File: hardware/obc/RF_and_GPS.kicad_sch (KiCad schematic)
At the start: 15 parts, among them J602 SMA RA Connector, J603 SMA RA Connector, J604 SMA RA Connector, U102 BMI088, U601 RFM98PW, U602 S1216V8, U603 GP2S1+

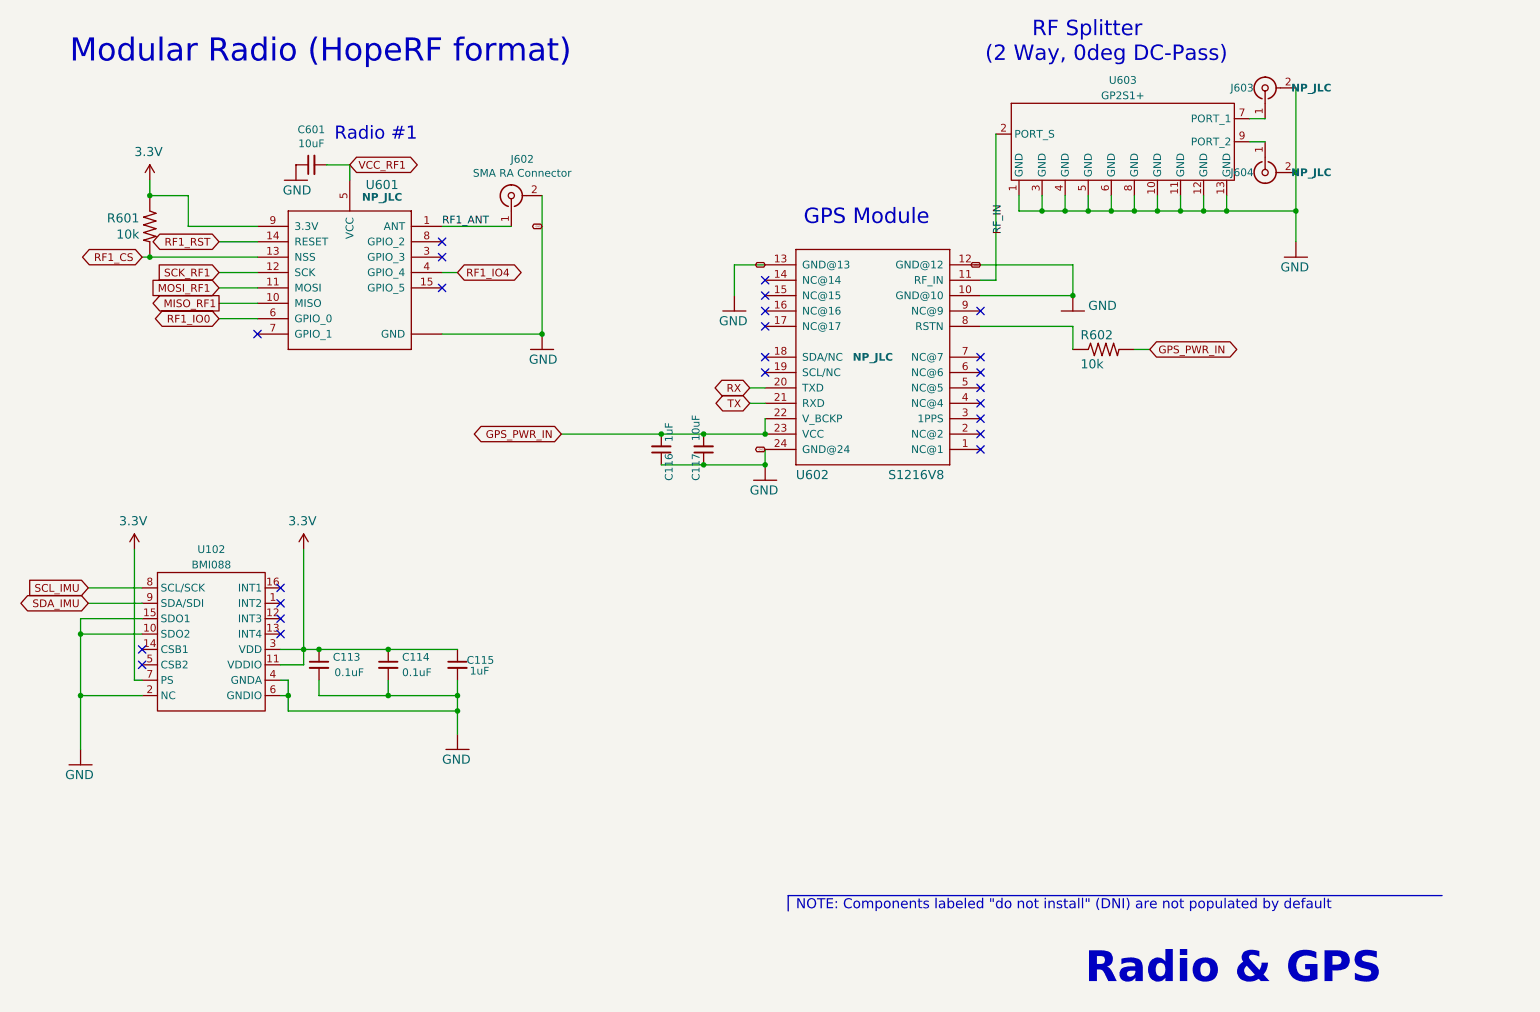
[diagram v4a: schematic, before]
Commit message: obc: refactors and renumbers
- renumber pages for more logical review order
- renumber reference designators to get smaller numbers
- small changes to layout from early design review
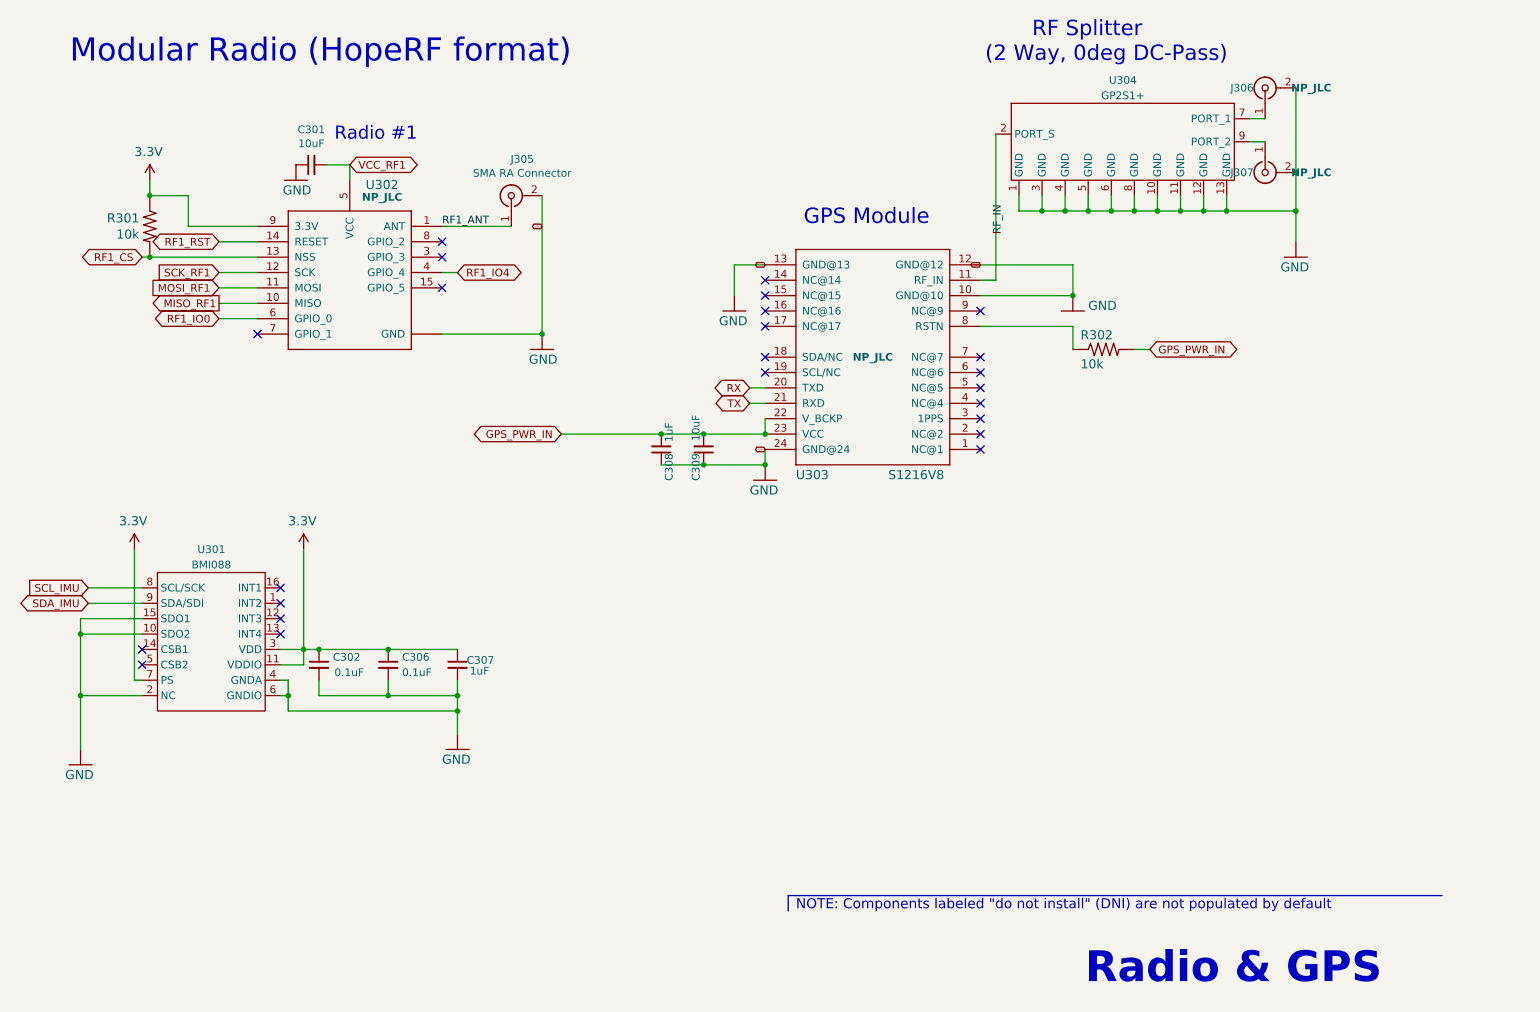
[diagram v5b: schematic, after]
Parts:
- renumbered C601 to C301, C113 to C302, C114 to C306, C115 to C307, C116 to C308, C117 to C309, J602 to J305, J603 to J306, J604 to J307, R601 to R301, R602 to R302, U102 to U301, U601 to U302, U602 to U303, U603 to U304
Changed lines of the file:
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@@
 		(on_board yes)
 		(dnp no)
-		(property "Reference" "R602"
+		(property "Reference" "R302"
 			(at 207.01 77.2414 0)
 			(effects
@@
 			(project "mainboard"
 				(path "/e3ac22ea-6806-4807-a025-571315789c25/00000000-0000-0000-0000-00005cec6281"
-					(reference "R602")
+					(reference "R302")
 					(unit 1)
 				)
@@
 		(on_board yes)
 		(dnp no)
-		(property "Reference" "#GND0607"
+		(property "Reference" "#GND0309"
 			(at 242.57 63.5 0)
 			(effects
@@
 			(project "mainboard"
 				(path "/e3ac22ea-6806-4807-a025-571315789c25/00000000-0000-0000-0000-00005cec6281"
-					(reference "#GND0607")
+					(reference "#GND0309")
 					(unit 1)
 				)
@@
 		(on_board yes)
 		(dnp no)
-		(property "Reference" "J603"
+		(property "Reference" "J306"
 			(at 233.68 35.56 90)
 			(effects
@@
 			(project "mainboard"
 				(path "/e3ac22ea-6806-4807-a025-571315789c25/00000000-0000-0000-0000-00005cec6281"
-					(reference "J603")
+					(reference "J306")
 					(unit 1)
 				)
@@
 		(on_board yes)
 		(dnp no)
-		(property "Reference" "J604"
+		(property "Reference" "J307"
 			(at 233.68 49.53 90)
 			(effects
@@
 			(project "mainboard"
 				(path "/e3ac22ea-6806-4807-a025-571315789c25/00000000-0000-0000-0000-00005cec6281"
-					(reference "J604")
+					(reference "J307")
 					(unit 1)
 				)
@@
 		(on_board yes)
 		(dnp no)
-		(property "Reference" "J602"
+		(property "Reference" "J305"
 			(at 114.8334 47.3202 90)
 			(effects
@@
 			(project "mainboard"
 				(path "/e3ac22ea-6806-4807-a025-571315789c25/00000000-0000-0000-0000-00005cec6281"
-					(reference "J602")
+					(reference "J305")
 					(unit 1)
 				)
@@
 		(on_board yes)
 		(dnp no)
-		(property "Reference" "U601"
+		(property "Reference" "U302"
 			(at 91.694 51.562 0)
 			(effects
@@
 			(project "mainboard"
 				(path "/e3ac22ea-6806-4807-a025-571315789c25/00000000-0000-0000-0000-00005cec6281"
-					(reference "U601")
+					(reference "U302")
 					(unit 1)
 				)
@@
 		(on_board yes)
 		(dnp no)
-		(property "Reference" "#GND0603"
+		(property "Reference" "#GND0305"
 			(at 118.11 78.74 0)
 			(effects
@@
 			(project "mainboard"
 				(path "/e3ac22ea-6806-4807-a025-571315789c25/00000000-0000-0000-0000-00005cec6281"
-					(reference "#GND0603")
+					(reference "#GND0305")
 					(unit 1)
 				)
@@
 		(on_board yes)
 		(dnp no)
-		(property "Reference" "R601"
+		(property "Reference" "R301"
 			(at 51.6128 57.0738 90)
 			(effects
@@
 			(project "mainboard"
 				(path "/e3ac22ea-6806-4807-a025-571315789c25/00000000-0000-0000-0000-00005cec6281"
-					(reference "R601")
+					(reference "R301")
 					(unit 1)
 				)
@@
 		(on_board yes)
 		(dnp no)
-		(property "Reference" "#SUPPLY0601"
+		(property "Reference" "#SUPPLY0302"
 			(at 53.34 50.8 0)
 			(effects
@@
 			(project "mainboard"
 				(path "/e3ac22ea-6806-4807-a025-571315789c25/00000000-0000-0000-0000-00005cec6281"
-					(reference "#SUPPLY0601")
+					(reference "#SUPPLY0302")
 					(unit 1)
 				)
@@
 		(on_board yes)
 		(dnp no)
-		(property "Reference" "C601"
+		(property "Reference" "C301"
 			(at 80.01 42.4434 90)
 			(effects
@@
 			(project "mainboard"
 				(path "/e3ac22ea-6806-4807-a025-571315789c25/00000000-0000-0000-0000-00005cec6281"
-					(reference "C601")
+					(reference "C301")
 					(unit 1)
 				)
@@
 		(on_board yes)
 		(dnp no)
-		(property "Reference" "#GND0601"
+		(property "Reference" "#GND0302"
 			(at 77.47 50.8 0)
 			(effects
@@
 			(project "mainboard"
 				(path "/e3ac22ea-6806-4807-a025-571315789c25/00000000-0000-0000-0000-00005cec6281"
-					(reference "#GND0601")
+					(reference "#GND0302")
 					(unit 1)
 				)
@@
 		(on_board yes)
 		(dnp no)
-		(property "Reference" "#GND0604"
+		(property "Reference" "#GND0306"
 			(at 149.86 72.39 0)
 			(effects
@@
 			(project "mainboard"
 				(path "/e3ac22ea-6806-4807-a025-571315789c25/00000000-0000-0000-0000-00005cec6281"
-					(reference "#GND0604")
+					(reference "#GND0306")
 					(unit 1)
 				)
@@
 		(on_board yes)
 		(dnp no)
-		(property "Reference" "#GND0605"
+		(property "Reference" "#GND0307"
 			(at 154.94 100.33 0)
 			(effects
@@
 			(project "mainboard"
 				(path "/e3ac22ea-6806-4807-a025-571315789c25/00000000-0000-0000-0000-00005cec6281"
-					(reference "#GND0605")
+					(reference "#GND0307")
 					(unit 1)
 				)
@@
 		(on_board yes)
 		(dnp no)
-		(property "Reference" "#GND0606"
+		(property "Reference" "#GND0308"
 			(at 205.74 72.39 0)
 			(effects
@@
 			(project "mainboard"
 				(path "/e3ac22ea-6806-4807-a025-571315789c25/00000000-0000-0000-0000-00005cec6281"
-					(reference "#GND0606")
+					(reference "#GND0308")
 					(unit 1)
 				)
@@
 		(on_board yes)
 		(dnp no)
-		(property "Reference" "U602"
+		(property "Reference" "U303"
 			(at 160.02 100.33 0)
 			(effects
@@
 			(project "mainboard"
 				(path "/e3ac22ea-6806-4807-a025-571315789c25/00000000-0000-0000-0000-00005cec6281"
-					(reference "U602")
+					(reference "U303")
 					(unit 1)
 				)
@@
 		(on_board yes)
 		(dnp no)
-		(property "Reference" "C114"
+		(property "Reference" "C306"
 			(at 94.996 129.54 0)
 			(effects
@@
 			(project "mainboard"
 				(path "/e3ac22ea-6806-4807-a025-571315789c25/00000000-0000-0000-0000-00005cec6281"
-					(reference "C114")
+					(reference "C306")
 					(unit 1)
 				)
@@
 		(on_board yes)
 		(dnp no)
-		(property "Reference" "U102"
+		(property "Reference" "U301"
 			(at 63.5 111.76 0)
 			(effects
@@
 			(project "mainboard"
 				(path "/e3ac22ea-6806-4807-a025-571315789c25/00000000-0000-0000-0000-00005cec6281"
-					(reference "U102")
+					(reference "U301")
 					(unit 1)
 				)
@@
 		(dnp no)
 		(fields_autoplaced yes)
-		(property "Reference" "U603"
+		(property "Reference" "U304"
 			(at 213.995 34.29 0)
 			(effects
@@
 			(project "mainboard"
 				(path "/e3ac22ea-6806-4807-a025-571315789c25/00000000-0000-0000-0000-00005cec6281"
-					(reference "U603")
+					(reference "U304")
 					(unit 1)
 				)
@@
 		(on_board yes)
 		(dnp no)
-		(property "Reference" "#SUPPLY0108"
+		(property "Reference" "#SUPPLY0301"
 			(at 50.8 111.76 0)
 			(effects
@@
 			(project "mainboard"
 				(path "/e3ac22ea-6806-4807-a025-571315789c25/00000000-0000-0000-0000-00005cec6281"
-					(reference "#SUPPLY0108")
+					(reference "#SUPPLY0301")
 					(unit 1)
 				)
@@
 		(on_board yes)
 		(dnp no)
-		(property "Reference" "C117"
+		(property "Reference" "C309"
 			(at 143.51 95.885 90)
 			(effects
@@
 			(project "mainboard"
 				(path "/e3ac22ea-6806-4807-a025-571315789c25/00000000-0000-0000-0000-00005cec6281"
-					(reference "C117")
+					(reference "C309")
 					(unit 1)
 				)
@@
 		(on_board yes)
 		(dnp no)
-		(property "Reference" "C113"
+		(property "Reference" "C302"
 			(at 83.566 129.54 0)
 			(effects
@@
 			(project "mainboard"
 				(path "/e3ac22ea-6806-4807-a025-571315789c25/00000000-0000-0000-0000-00005cec6281"
-					(reference "C113")
+					(reference "C302")
 					(unit 1)
 				)
@@
 		(on_board yes)
 		(dnp no)
-		(property "Reference" "#GND0111"
+		(property "Reference" "#GND0301"
 			(at 41.91 147.32 0)
 			(effects
@@
 			(project "mainboard"
 				(path "/e3ac22ea-6806-4807-a025-571315789c25/00000000-0000-0000-0000-00005cec6281"
-					(reference "#GND0111")
+					(reference "#GND0301")
 					(unit 1)
 				)
@@
 		(on_board yes)
 		(dnp no)
-		(property "Reference" "C115"
+		(property "Reference" "C307"
 			(at 105.664 130.048 0)
 			(effects
@@
 			(project "mainboard"
 				(path "/e3ac22ea-6806-4807-a025-571315789c25/00000000-0000-0000-0000-00005cec6281"
-					(reference "C115")
+					(reference "C307")
 					(unit 1)
 				)
@@
 		(on_board yes)
 		(dnp no)
-		(property "Reference" "#SUPPLY0110"
+		(property "Reference" "#SUPPLY0303"
 			(at 78.74 111.76 0)
 			(effects
@@
 			(project "mainboard"
 				(path "/e3ac22ea-6806-4807-a025-571315789c25/00000000-0000-0000-0000-00005cec6281"
-					(reference "#SUPPLY0110")
+					(reference "#SUPPLY0303")
 					(unit 1)
 				)
@@
 		(on_board yes)
 		(dnp no)
-		(property "Reference" "#GND0112"
+		(property "Reference" "#GND0303"
 			(at 104.14 144.78 0)
 			(effects
@@
 			(project "mainboard"
 				(path "/e3ac22ea-6806-4807-a025-571315789c25/00000000-0000-0000-0000-00005cec6281"
-					(reference "#GND0112")
+					(reference "#GND0303")
 					(unit 1)
 				)
@@
 		(on_board yes)
 		(dnp no)
-		(property "Reference" "C116"
+		(property "Reference" "C308"
 			(at 139.065 95.885 90)
 			(effects
@@
 			(project "mainboard"
 				(path "/e3ac22ea-6806-4807-a025-571315789c25/00000000-0000-0000-0000-00005cec6281"
-					(reference "C116")
+					(reference "C308")
 					(unit 1)
 				)

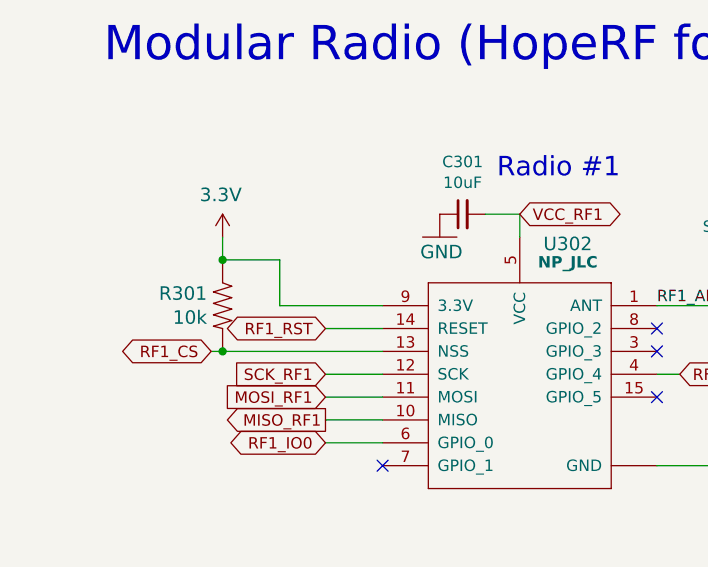
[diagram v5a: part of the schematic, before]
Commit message: obc: rename power nets for sanity
We've been confused by this for too long.

GNDREF -> PACKNEG
VCHRG -> PACKPOS
VBATT -> VRAIL
VBATT_SENSE -> INH_POS

Also add an OBC power subsystem diagram.
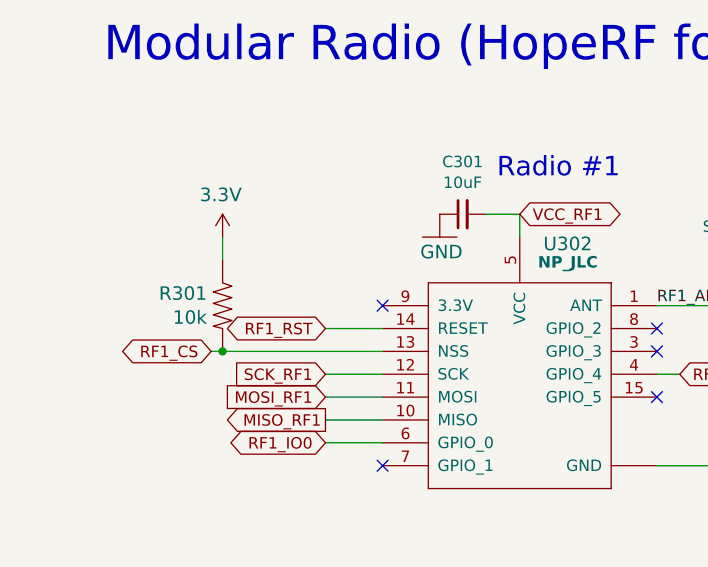
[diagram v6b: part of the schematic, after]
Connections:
- net 3.3V: no longer U302.9 (3.3V)
- no-connect marks 24 -> 25
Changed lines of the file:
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@@
-	)
-	(junction
-		(at 53.34 53.34)
-		(diameter 0)
-		(color 0 0 0 0)
 	)
 	(junction
@@
 	)
 	(no_connect
+		(at 71.12 58.42)
+	)
+	(no_connect
 		(at 101.6 63.5)
 	)
@@
 	(wire
 		(pts
-			(xy 71.12 58.42) (xy 59.69 58.42)
-		)
-		(stroke
-			(width 0)
-			(type default)
-		)
-	)
-	(wire
-		(pts
 			(xy 204.47 55.88) (xy 200.66 55.88)
 		)
@@
 	(wire
 		(pts
-			(xy 59.69 53.34) (xy 53.34 53.34)
-		)
-		(stroke
-			(width 0)
-			(type default)
-		)
-	)
-	(wire
-		(pts
 			(xy 71.12 68.58) (xy 64.77 68.58)
 		)
@@
 		)
 		(stroke
-			(width 0)
-			(type default)
-		)
-	)
-	(wire
-		(pts
-			(xy 59.69 58.42) (xy 59.69 53.34)
-		)
-		(stroke
